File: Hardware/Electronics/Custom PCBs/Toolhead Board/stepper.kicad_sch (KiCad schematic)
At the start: 13 parts, among them J4 MOTOR, U6 TMC2209-LA

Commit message: Make some updates
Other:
- moved on the sheet: J4
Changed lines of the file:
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@@
     (stroke (width 0) (type default))
   )
-  (wire (pts (xy 200.66 74.93) (xy 207.01 74.93))
-    (stroke (width 0) (type default))
-  )
-  (wire (pts (xy 200.66 77.47) (xy 207.01 77.47))
+  (wire (pts (xy 186.69 71.12) (xy 193.04 71.12))
+    (stroke (width 0) (type default))
+  )
+  (wire (pts (xy 186.69 73.66) (xy 193.04 73.66))
     (stroke (width 0) (type default))
   )
@@
     (stroke (width 0) (type default))
   )
-  (wire (pts (xy 200.66 72.39) (xy 207.01 72.39))
+  (wire (pts (xy 186.69 68.58) (xy 193.04 68.58))
     (stroke (width 0) (type default))
   )
@@
     (stroke (width 0) (type default))
   )
-  (wire (pts (xy 200.66 80.01) (xy 207.01 80.01))
+  (wire (pts (xy 186.69 76.2) (xy 193.04 76.2))
     (stroke (width 0) (type default))
   )
@@
     (stroke (width 0) (type default))
   )
-  (label "OA2" (at 200.66 72.39 0) (fields_autoplaced)
+  (label "OA2" (at 186.69 68.58 0) (fields_autoplaced)
     (effects (font (size 1.27 1.27)) (justify left bottom))
   )
@@
     (effects (font (size 1.27 1.27)) (justify left bottom))
   )
-  (label "OB2" (at 200.66 80.01 0) (fields_autoplaced)
+  (label "OB2" (at 186.69 76.2 0) (fields_autoplaced)
     (effects (font (size 1.27 1.27)) (justify left bottom))
   )
@@
     (effects (font (size 1.27 1.27)) (justify right bottom))
   )
-  (label "OA1" (at 200.66 74.93 0) (fields_autoplaced)
+  (label "OA1" (at 186.69 71.12 0) (fields_autoplaced)
     (effects (font (size 1.27 1.27)) (justify left bottom))
   )
@@
     (effects (font (size 1.27 1.27)) (justify left bottom))
   )
-  (label "OB1" (at 200.66 77.47 0) (fields_autoplaced)
+  (label "OB1" (at 186.69 73.66 0) (fields_autoplaced)
     (effects (font (size 1.27 1.27)) (justify left bottom))
   )
@@
     )
   )
-  (symbol (lib_id "Connector_Generic:Conn_01x04") (at 212.09 74.93 0) (unit 1)
-    (in_bom yes) (on_board yes) (dnp no) (fields_autoplaced)
-    (property "Reference" "J4" (at 214.63 74.93 0)
+  (symbol (lib_id "Connector_Generic:Conn_01x04") (at 198.12 71.12 0) (unit 1)
+    (in_bom yes) (on_board yes) (dnp no) (fields_autoplaced)
+    (property "Reference" "J4" (at 200.66 71.12 0)
       (effects (font (size 1.27 1.27)) (justify left))
     )
-    (property "Value" "MOTOR" (at 214.63 77.47 0)
+    (property "Value" "MOTOR" (at 200.66 73.66 0)
       (effects (font (size 1.27 1.27)) (justify left))
     )
-    (property "Footprint" "Connector_JST:JST_PH_S4B-PH-K_1x04_P2.00mm_Horizontal" (at 212.09 74.93 0)
-      (effects (font (size 1.27 1.27)) hide)
-    )
-    (property "Datasheet" "~" (at 212.09 74.93 0)
-      (effects (font (size 1.27 1.27)) hide)
-    )
+    (property "Footprint" "Connector_JST:JST_PH_S4B-PH-K_1x04_P2.00mm_Horizontal" (at 198.12 71.12 0)
+      (effects (font (size 1.27 1.27)) hide)
+    )
+    (property "Datasheet" "~" (at 198.12 71.12 0)
+      (effects (font (size 1.27 1.27)) hide)
+    )

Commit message: some updates
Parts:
- J4: footprint Connector_JST:JST_PH_S4B-PH-K_1x04_P2.00mm_Horizontal -> (none)
- U6: footprint QFN28_5X5_TRI -> (none); Digikey (none) -> 505-TMC2209-LA-ND
- renumbered C26 to C24, C24 to C26, C29 to C27, C30 to C28, C28 to C29, C27 to C30, R14 to R12, R12 to R14

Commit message: Work on toolhead board more
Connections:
- net MOT_DIAG: now reaches JP1.1 (A)
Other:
- moved on the sheet: C28
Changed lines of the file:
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@@
   (junction (at 179.07 66.04) (diameter 0) (color 0 0 0 0)
+  )
+  (junction (at 57.15 73.66) (diameter 0) (color 0 0 0 0)
   )
   (junction (at 119.38 24.13) (diameter 0) (color 0 0 0 0)
@@
     (stroke (width 0) (type default))
   )
-  (wire (pts (xy 62.23 73.66) (xy 93.98 73.66))
+  (wire (pts (xy 52.07 73.66) (xy 57.15 73.66))
+    (stroke (width 0) (type default))
+  )
+  (wire (pts (xy 57.15 73.66) (xy 93.98 73.66))
     (stroke (width 0) (type default))
   )
@@
     (effects (font (size 1.27 1.27)) (justify right))
     (property "Intersheetrefs" "${INTERSHEET_REFS}" (at 83.7982 63.5 0)
+      (effects (font (size 1.27 1.27)) (justify right) hide)
+    )
+  )
+  (global_label "MOT_DIAG" (shape input) (at 50.8 95.25 180) (fields_autoplaced)
+    (effects (font (size 1.27 1.27)) (justify right))
+    (property "Intersheetrefs" "${INTERSHEET_REFS}" (at 38.8643 95.25 0)
       (effects (font (size 1.27 1.27)) (justify right) hide)
     )
@@
     )
   )
-  (symbol (lib_id "Device:C") (at 58.42 73.66 90) (unit 1)
-    (in_bom yes) (on_board yes) (dnp no) (fields_autoplaced)
-    (property "Reference" "C28" (at 58.42 66.04 90)
+  (symbol (lib_id "power:PWR_FLAG") (at 57.15 73.66 0) (unit 1)
+    (in_bom yes) (on_board yes) (dnp no)
+    (property "Reference" "#FLG05" (at 57.15 71.755 0)
+      (effects (font (size 1.27 1.27)) hide)
+    )
+    (property "Value" "PWR_FLAG" (at 57.15 64.77 90)
       (effects (font (size 1.27 1.27)))
     )
-    (property "Value" "100n" (at 58.42 68.58 90)
+    (property "Footprint" "" (at 57.15 73.66 0)
+      (effects (font (size 1.27 1.27)) hide)
+    )
+    (property "Datasheet" "~" (at 57.15 73.66 0)
+      (effects (font (size 1.27 1.27)) hide)
+    )
+    (pin "1")
+    (instances
+      (project "Toolhead Board"
+        (path "/a1747683-152e-4245-ab61-2d33ce6021ef/1af119c3-7c67-4253-a987-5e4038b04e95"
+          (reference "#FLG05") (unit 1)
+        )
+      )
+    )
+  )
+  (symbol (lib_id "Device:C") (at 48.26 73.66 90) (unit 1)
+    (in_bom yes) (on_board yes) (dnp no) (fields_autoplaced)
+    (property "Reference" "C28" (at 48.26 66.04 90)
       (effects (font (size 1.27 1.27)))
     )
-    (property "Footprint" "" (at 62.23 72.6948 0)
-      (effects (font (size 1.27 1.27)) hide)
-    )
-    (property "Datasheet" "~" (at 58.42 73.66 0)
-      (effects (font (size 1.27 1.27)) hide)
-    )
-    (property "Digikey" "" (at 58.42 73.66 0)
+    (property "Value" "100n" (at 48.26 68.58 90)
+      (effects (font (size 1.27 1.27)))
+    )
+    (property "Footprint" "" (at 52.07 72.6948 0)
+      (effects (font (size 1.27 1.27)) hide)
+    )
+    (property "Datasheet" "~" (at 48.26 73.66 0)
+      (effects (font (size 1.27 1.27)) hide)
+    )
+    (property "Digikey" "" (at 48.26 73.66 0)
       (effects (font (size 1.27 1.27)) hide)
     )
@@
     )
   )
-  (symbol (lib_id "power:+24V") (at 54.61 73.66 90) (unit 1)
-    (in_bom yes) (on_board yes) (dnp no) (fields_autoplaced)
-    (property "Reference" "#PWR038" (at 58.42 73.66 0)
-      (effects (font (size 1.27 1.27)) hide)
-    )
-    (property "Value" "+24V" (at 50.8 73.66 90)
+  (symbol (lib_id "power:+24V") (at 44.45 73.66 90) (unit 1)
+    (in_bom yes) (on_board yes) (dnp no) (fields_autoplaced)
+    (property "Reference" "#PWR038" (at 48.26 73.66 0)
+      (effects (font (size 1.27 1.27)) hide)
+    )
+    (property "Value" "+24V" (at 40.64 73.66 90)
       (effects (font (size 1.27 1.27)) (justify left))
     )
-    (property "Footprint" "" (at 54.61 73.66 0)
-      (effects (font (size 1.27 1.27)) hide)
-    )
-    (property "Datasheet" "" (at 54.61 73.66 0)
-      (effects (font (size 1.27 1.27)) hide)
-    )
+    (property "Footprint" "" (at 44.45 73.66 0)
+      (effects (font (size 1.27 1.27)) hide)
+    )
+    (property "Datasheet" "" (at 44.45 73.66 0)
+      (effects (font (size 1.27 1.27)) hide)
+    )

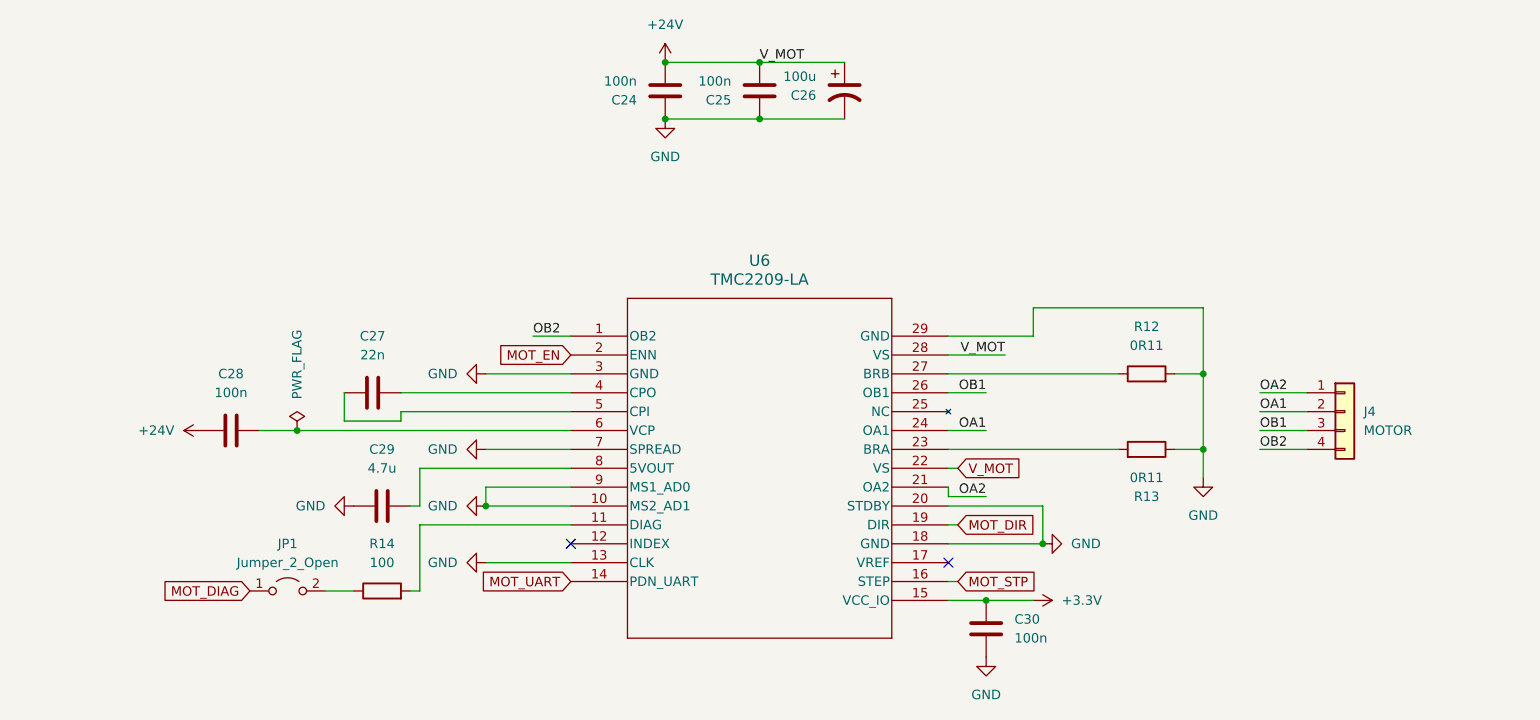
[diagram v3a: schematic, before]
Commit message: Finish Toolhead Schematic
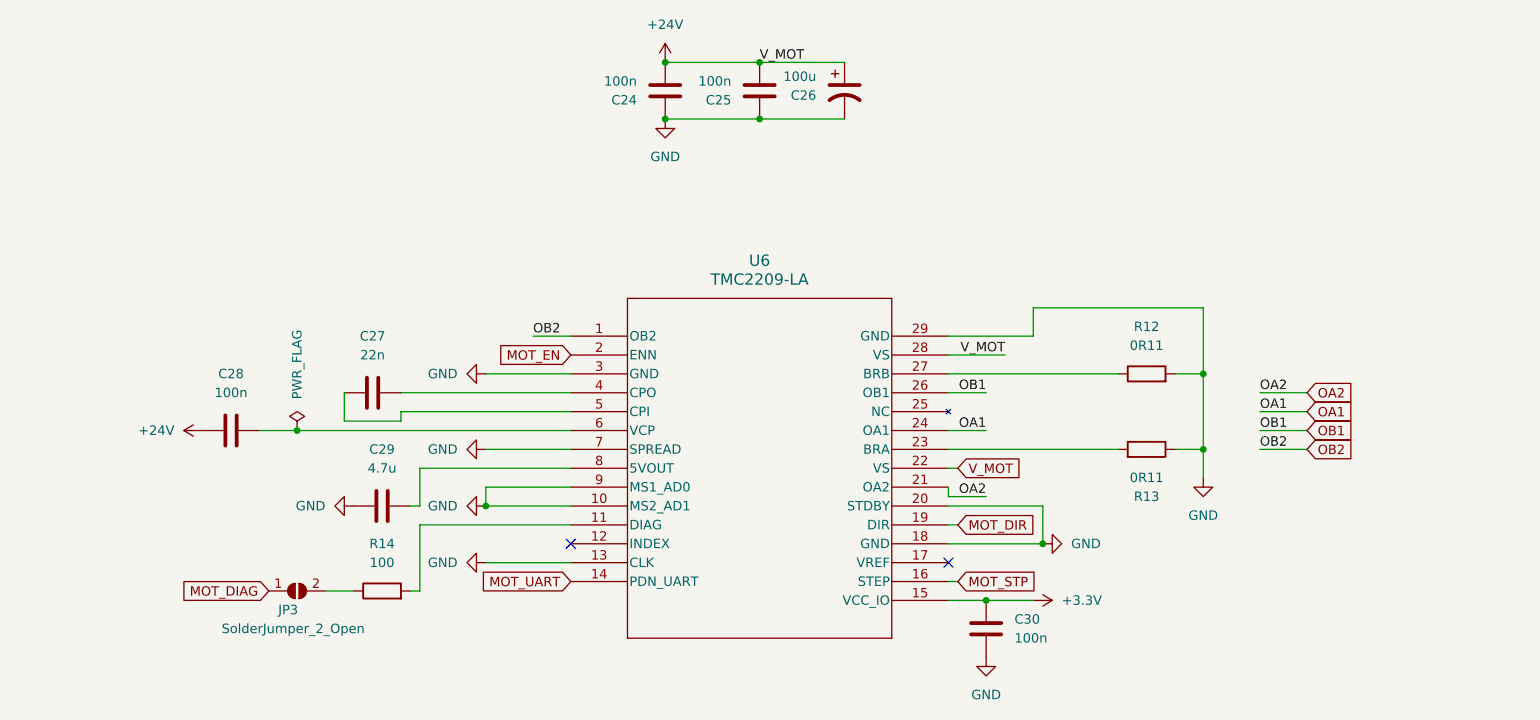
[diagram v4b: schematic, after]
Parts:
- removed J4: MOTOR, symbol Connector_Generic:Conn_01x04
- removed JP1: Jumper_2_Open, symbol Jumper:Jumper_2_Open
- added JP3: SolderJumper_2_Open, symbol Jumper:SolderJumper_2_Open
- C24, C25, C28, C30: Digikey (none) -> 1276-1935-1-ND
- C26: Digikey (none) -> 495-5984-ND
- C27: Digikey (none) -> 1292-1417-1-ND
- C29: Digikey (none) -> 1276-1044-1-ND
- R12, R13: footprint (none) -> Resistor_SMD:R_0603_1608Metric_Pad0.98x0.95mm_HandSolder
- R14: footprint (none) -> Resistor_SMD:R_0603_1608Metric_Pad0.98x0.95mm_HandSolder; Digikey (none) -> 311-100HRCT-ND
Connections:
- net MOT_DIAG: now also JP3.1 (A)
- net at R14.1: now also JP3.2 (B)

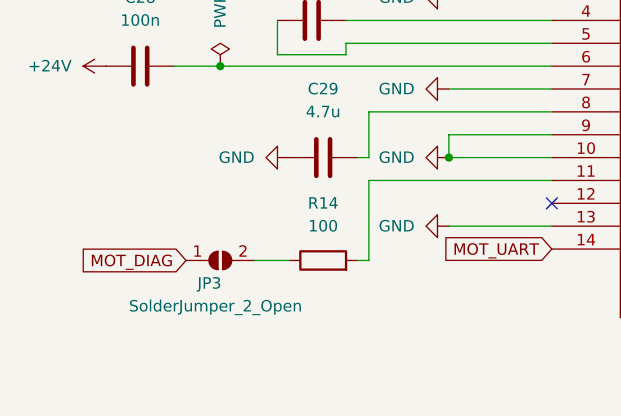
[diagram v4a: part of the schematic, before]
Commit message: Updated Footprints
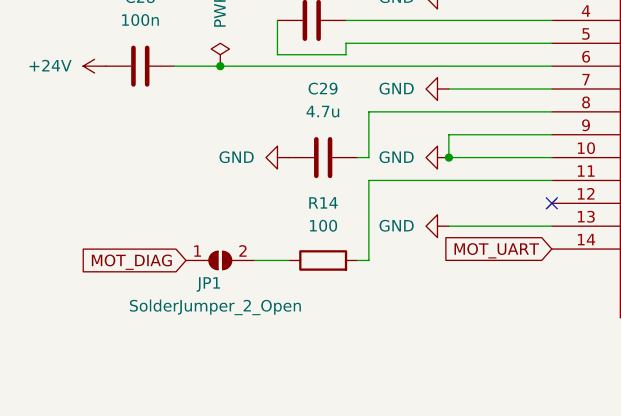
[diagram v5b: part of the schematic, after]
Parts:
- C24, C25, C28, C30: footprint (none) -> Capacitor_SMD:C_0603_1608Metric_Pad1.08x0.95mm_HandSolder
- U6: footprint (none) -> Package_DFN_QFN:QFN-28-1EP_5x5mm_P0.5mm_EP3.75x3.75mm_ThermalVias
- renumbered JP3 to JP1

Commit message: Continue adding footprints
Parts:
- C26: footprint (none) -> Capacitor_THT:CP_Radial_D8.0mm_P3.50mm
- C27, C29: footprint (none) -> Capacitor_SMD:C_0603_1608Metric_Pad1.08x0.95mm_HandSolder
- JP1: footprint (none) -> Jumper:SolderJumper-2_P1.3mm_Open_RoundedPad1.0x1.5mm
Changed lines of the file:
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@@
 			)
 		)
-		(property "Footprint" ""
+		(property "Footprint" "Capacitor_THT:CP_Radial_D8.0mm_P3.50mm"
 			(at 130.81 27.94 0)
 			(effects
@@
 			)
 		)
-		(property "Footprint" ""
+		(property "Footprint" "Capacitor_SMD:C_0603_1608Metric_Pad1.08x0.95mm_HandSolder"
 			(at 72.39 82.8548 0)
 			(effects
@@
 			)
 		)
-		(property "Footprint" ""
+		(property "Footprint" "Capacitor_SMD:C_0603_1608Metric_Pad1.08x0.95mm_HandSolder"
 			(at 71.12 67.6148 0)
 			(effects
@@
 			)
 		)
-		(property "Footprint" ""
+		(property "Footprint" "Jumper:SolderJumper-2_P1.3mm_Open_RoundedPad1.0x1.5mm"
 			(at 57.15 95.25 0)
 			(effects
